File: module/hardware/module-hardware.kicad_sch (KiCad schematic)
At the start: 26 parts

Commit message: Add loopback routing mux; add digital signals to headers
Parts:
- added R?: 10k, symbol Device:R
- U6: renamed from U?; footprint (none) -> Package_SO:VSSOP-8_2.3x2mm_P0.5mm
- gave numbers to parts that had none: 25
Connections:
- net GNDD is gone; now on net GND: C1.2, C10.2, C2.2, C3.2, C4.2, C9.2, J1.5 (GND), J1.6 (Shield), J2.22 (Pin_22), J2.23 (Pin_23), J2.26 (Pin_26), J2.27 (Pin_27), J2.30 (Pin_30), J2.31 (Pin_31), J2.34 (Pin_34), J2.35 (Pin_35), J2.38 (Pin_38), J2.39 (Pin_39), SW1.1, U1.1 (GND), U4.10 (DGND)
- net VCC is gone; now on net +3V3: U6.8 (VCC)
- net +5VD: now also J2.32 (Pin_32), J4.24 (Pin_24), J4.25 (Pin_25)
- net GND: now also J4.22 (Pin_22), J4.23 (Pin_23), J4.26 (Pin_26), J4.27 (Pin_27), J4.30 (Pin_30), J4.31 (Pin_31), J4.34 (Pin_34), J4.35 (Pin_35), J4.38 (Pin_38), J4.39 (Pin_39), U6.2, R?.2
- net CBUS_SDRETOUT: now reaches U6.1
- net CBUS_SDRETOUT: now also J2.29 (Pin_29)
- net CBUS_NEXTPRSNT: now reaches U6.5
- net CBUS_NEXTPRSNT: now also J4.32 (Pin_32), R?.1
- net CBUS_SDRETIN: now reaches U6.6
- net CBUS_SDRETIN: now also J4.29 (Pin_29)
- net CBUS_SDOUT: now reaches U6.7
- net CBUS_SDOUT: now also J4.33 (Pin_33)
- net CBUS_SCK: now reaches J4.36 (Pin_36)
- net CBUS_SCK: now also J2.36 (Pin_36)
- net CBUS_DRDY: now reaches J4.37 (Pin_37)
- net CBUS_DRDY: now also J2.37 (Pin_37)
- net CBUS_EXTRA: now reaches J4.40 (Pin_40)
- net CBUS_EXTRA: now also J2.40 (Pin_40)
- net CBUS_SDIN: now reaches J2.33 (Pin_33)
- no-connect marks 1 -> 3
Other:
- sheet D.R.U.M. Module Digital ports: added GPIO16_EXTRA, GPIO17_DRDY, GPIO18_SCK, GPIO19_SDIN, GPIO20_SDOUT; removed none
- note added: "Data bus loopback routing mux"
- moved on the sheet: J4, U6A

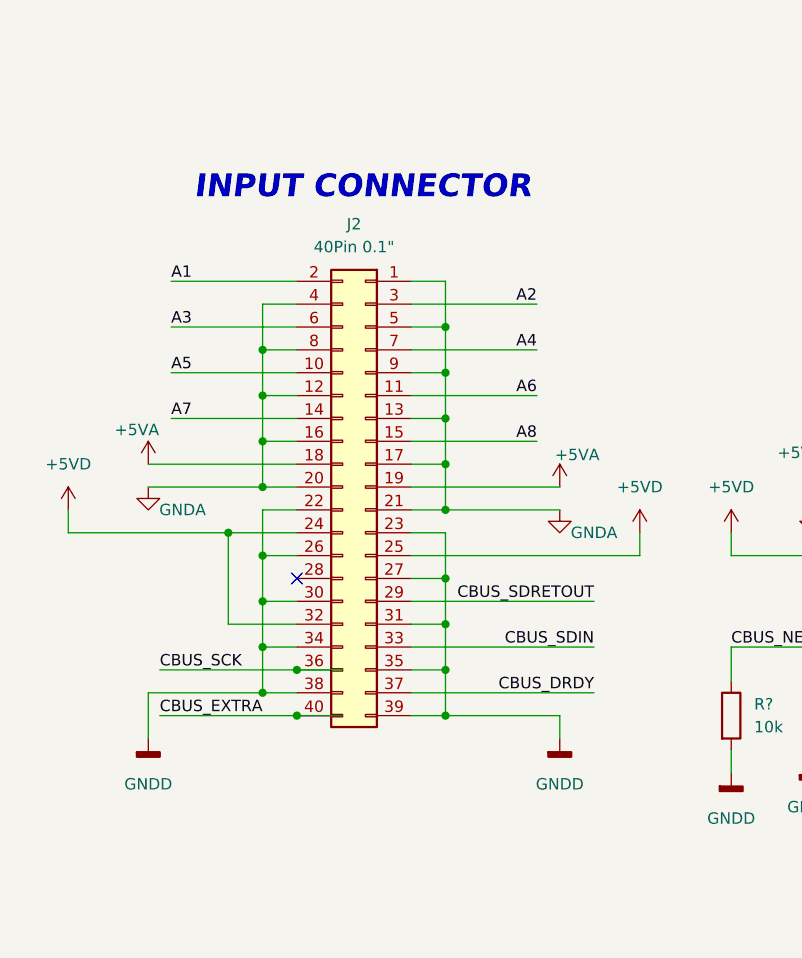
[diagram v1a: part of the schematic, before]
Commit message: Added pull-down resistors to analog passthroughs
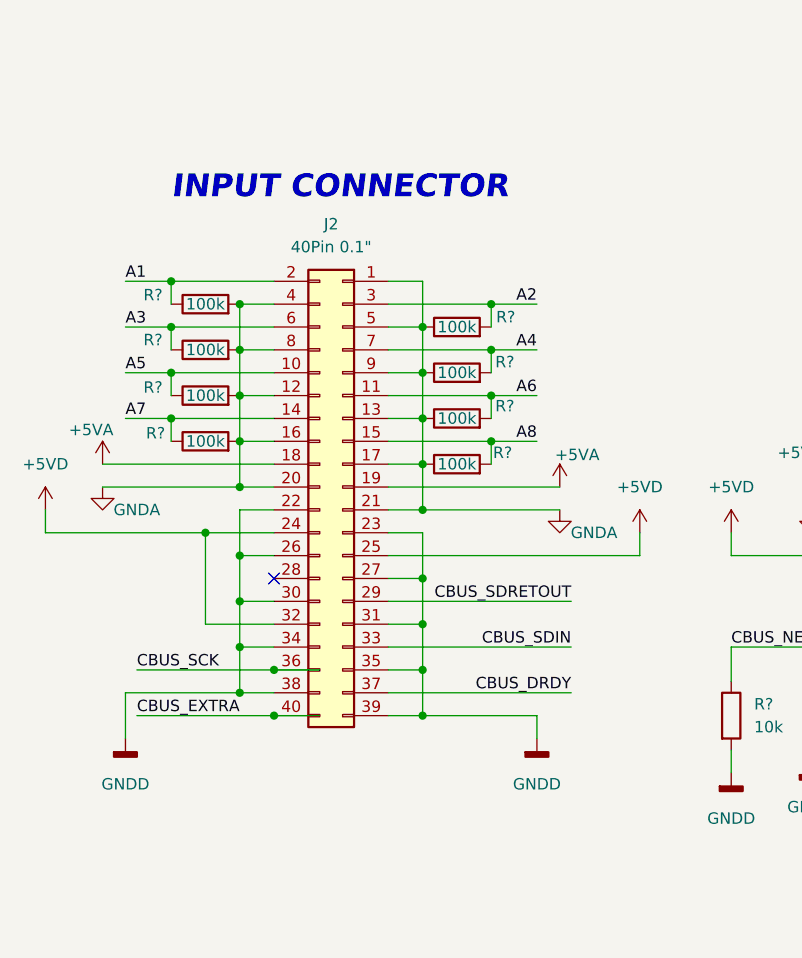
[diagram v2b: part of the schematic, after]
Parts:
- added R? (x8): 100k, symbol Device:R
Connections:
- net A1: now also R?.1
- net A2: now also R?.2
- net A3: now also R?.1
- net A4: now also R?.2
- net A5: now also R?.1
- net A6: now also R?.2
- net A7: now also R?.1
- net A8: now also R?.2
- net GNDA: now also R?.1, R?.1, R?.1, R?.1, R?.2, R?.2, R?.2, R?.2
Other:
- moved on the sheet: J2

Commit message: Add ADC vref, encoder & button headers
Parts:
- added C10, C13, C9: 0.1u, symbol Device:C
- added U5: MAX6070, symbol custom-lib:MAX6070
- gave numbers to parts that had none: 9
- renumbered C9 to C11, C10 to C12, R1 to R10, R2 to R11, R3 to R12, R4 to R13, U6 to U4, U4 to U6, U5 to U7
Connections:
- net +3.3VA: now also C9.1, U5.3 (EN), U5.4 (IN)
- net +3V3: no longer U6.2 (REF)
- net GND: no longer U6.10 (DGND)
- net GNDA: now also U6.10 (DGND), C10.2, C13.2, C9.2, U5.2 (GND)
- new net: C13.1, U5.5 (OUTS), U5.6 (OUTF), U6.2 (REF)
- new net: C10.1, U5.1 (FILTER)
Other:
- note removed: "NOTE: AGND and DGND must be tied together at this point"
- moved on the sheet: C11, C12, RV1, U4A, U6, U7

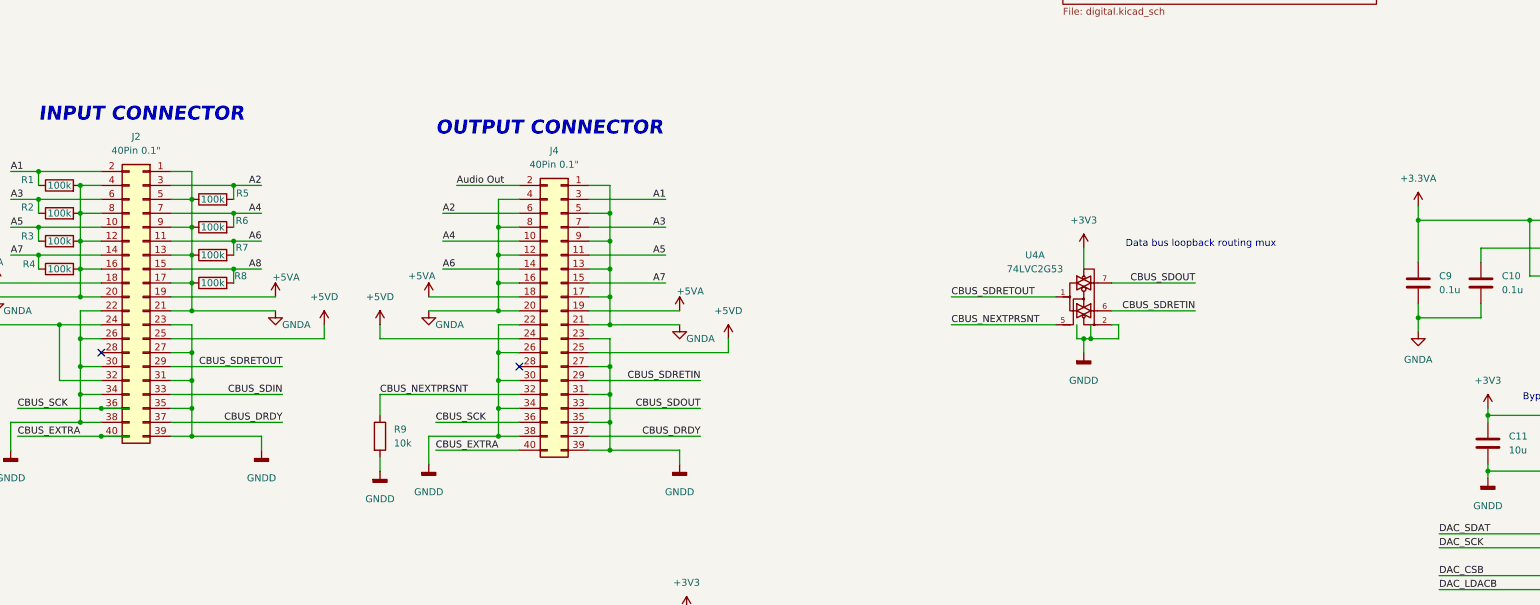
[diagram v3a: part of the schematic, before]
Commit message: Fix voltage rev supply (5V -> 3V3)
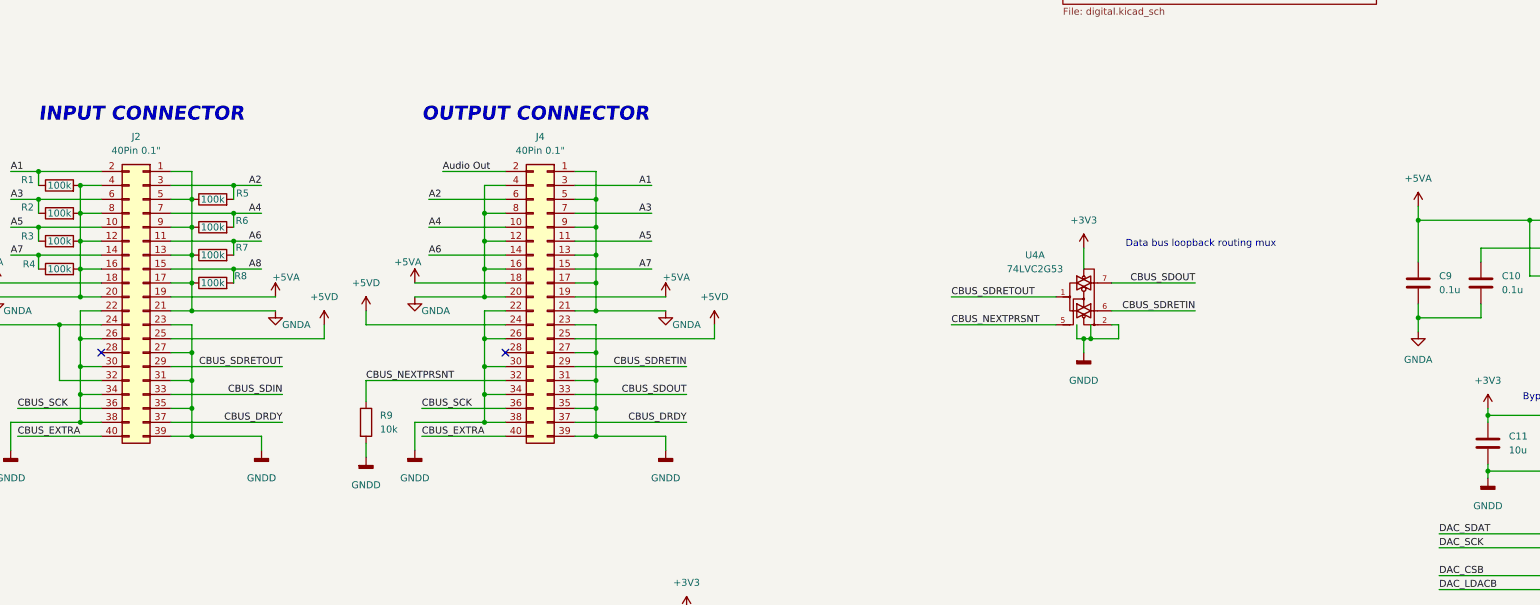
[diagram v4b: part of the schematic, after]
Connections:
- net +3.3VA: no longer C9.1, U5.3 (EN), U5.4 (IN)
- net +5VA: now also C9.1, U5.3 (EN), U5.4 (IN)
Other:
- moved on the sheet: J4, R9

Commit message: Add most footprints
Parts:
- C1, C11, C5: footprint (none) -> Capacitor_SMD:C_1206_3216Metric_Pad1.33x1.80mm_HandSolder
- C10, C12, C13, C2, C4, C6, C8, C9: footprint (none) -> Capacitor_SMD:C_0603_1608Metric_Pad1.08x0.95mm_HandSolder
- C3, C7: footprint (none) -> Capacitor_THT:CP_Radial_D8.0mm_P3.50mm
- J2: footprint (none) -> Connector_PinHeader_2.54mm:PinHeader_2x20_P2.54mm_Horizontal
- J3: footprint (none) -> Connector_PinHeader_2.54mm:PinHeader_1x02_P2.54mm_Horizontal
- J4: footprint (none) -> Connector_PinSocket_2.54mm:PinSocket_2x20_P2.54mm_Horizontal
- R1, R2, R3, R4, R5, R6, R7, R8: footprint (none) -> Resistor_SMD:R_1206_3216Metric_Pad1.30x1.75mm_HandSolder
- R10, R11, R13, R9: footprint (none) -> Resistor_SMD:R_0201_0603Metric_Pad0.64x0.40mm_HandSolder
- R12: footprint (none) -> Resistor_SMD:R_0603_1608Metric_Pad0.98x0.95mm_HandSolder
- U5: footprint (none) -> Package_TO_SOT_SMD:SOT-23-6_Handsoldering

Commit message: Finish footprint assignments; create cusom footprint lib
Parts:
- J1: footprint (none) -> Connector_USB:USB_Micro-B_Amphenol_10104110_Horizontal
- RV1: footprint (none) -> Potentiometer_THT:Potentiometer_Bourns_PTA6043_Single_Slide
- SW1: footprint (none) -> custom:TE_ConnMSLPT5252CG1
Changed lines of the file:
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@@
     (property "Reference" "SW1" (id 0) (at 139.7 199.39 0))
     (property "Value" "SW_Push" (id 1) (at 139.7 201.93 0))
-    (property "Footprint" "" (id 2) (at 139.7 201.93 0)
+    (property "Footprint" "custom:TE_ConnMSLPT5252CG1" (id 2) (at 139.7 201.93 0)
       (effects (font (size 1.27 1.27)) hide)
     )
@@
       (effects (font (size 1.27 1.27)) (justify right))
     )
-    (property "Footprint" "" (id 2) (at 360.68 171.45 0)
+    (property "Footprint" "Potentiometer_THT:Potentiometer_Bourns_PTA6043_Single_Slide" (id 2) (at 360.68 171.45 0)
       (effects (font (size 1.27 1.27)) hide)
     )
@@
     (property "Reference" "J1" (id 0) (at 31.75 190.5 0))
     (property "Value" "USB_B_Micro" (id 1) (at 31.75 193.04 0))
-    (property "Footprint" "" (id 2) (at 35.56 204.47 0)
+    (property "Footprint" "Connector_USB:USB_Micro-B_Amphenol_10104110_Horizontal" (id 2) (at 35.56 204.47 0)
       (effects (font (size 1.27 1.27)) hide)
     )
@@
     )
     (path "/c64d0991-6666-40ad-8f53-c4ec2d5065e9"
-      (reference "J1") (unit 1) (value "USB_B_Micro") (footprint "")
+      (reference "J1") (unit 1) (value "USB_B_Micro") (footprint "Connector_USB:USB_Micro-B_Amphenol_10104110_Horizontal")
     )
     (path "/d067ccfc-7346-4531-8a45-4ec88728c2e4"
@@
     )
     (path "/b169d545-bdb0-46f0-9e8e-232b739be3d3"
-      (reference "RV1") (unit 1) (value "10k Linear Pot") (footprint "")
+      (reference "RV1") (unit 1) (value "10k Linear Pot") (footprint "Potentiometer_THT:Potentiometer_Bourns_PTA6043_Single_Slide")
     )
     (path "/59c5fdd4-0275-4651-851a-34879fe6317f"
-      (reference "SW1") (unit 1) (value "SW_Push") (footprint "")
+      (reference "SW1") (unit 1) (value "SW_Push") (footprint "custom:TE_ConnMSLPT5252CG1")
     )
     (path "/8bf4dbf7-8f8f-435d-919b-c3a7dd1cb571/c3b0ca1c-76c1-4f22-a9a4-4f2d2d26349d"
-      (reference "SW2") (unit 1) (value "SW_Push") (footprint "")
+      (reference "SW2") (unit 1) (value "SW_Push") (footprint "custom:TE_ConnMSLPT5252CG1")
     )
     (path "/9c728db0-69af-414d-a337-b8d8f91d4481"

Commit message: Fix header footprints
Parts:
- J2: footprint Connector_PinHeader_2.54mm:PinHeader_2x20_P2.54mm_Horizontal -> Connector_PinSocket_2.54mm:PinSocket_2x20_P2.54mm_Horizontal
- J3: footprint Connector_PinHeader_2.54mm:PinHeader_1x02_P2.54mm_Horizontal -> Connector_PinHeader_2.54mm:PinHeader_1x02_P2.54mm_Vertical
- J4: footprint Connector_PinSocket_2.54mm:PinSocket_2x20_P2.54mm_Horizontal -> Connector_PinHeader_2.54mm:PinHeader_2x20_P2.54mm_Horizontal
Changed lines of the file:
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@@
     (property "Reference" "J4" (id 0) (at 123.19 88.9 0))
     (property "Value" "40Pin 0.1\"" (id 1) (at 123.19 91.44 0))
-    (property "Footprint" "Connector_PinSocket_2.54mm:PinSocket_2x20_P2.54mm_Horizontal" (id 2) (at 124.46 118.11 0)
+    (property "Footprint" "Connector_PinHeader_2.54mm:PinHeader_2x20_P2.54mm_Horizontal" (id 2) (at 124.46 118.11 0)
       (effects (font (size 1.27 1.27)) hide)
     )
@@
     (property "Reference" "J2" (id 0) (at 49.53 88.9 0))
     (property "Value" "40Pin 0.1\"" (id 1) (at 49.53 91.44 0))
-    (property "Footprint" "Connector_PinHeader_2.54mm:PinHeader_2x20_P2.54mm_Horizontal" (id 2) (at 50.8 118.11 0)
+    (property "Footprint" "Connector_PinSocket_2.54mm:PinSocket_2x20_P2.54mm_Horizontal" (id 2) (at 50.8 118.11 0)
       (effects (font (size 1.27 1.27)) hide)
     )
@@
       (effects (font (size 1.27 1.27)) (justify left))
     )
-    (property "Footprint" "Connector_PinHeader_2.54mm:PinHeader_1x02_P2.54mm_Horizontal" (id 2) (at 55.88 190.5 0)
+    (property "Footprint" "Connector_PinHeader_2.54mm:PinHeader_1x02_P2.54mm_Vertical" (id 2) (at 55.88 190.5 0)
       (effects (font (size 1.27 1.27)) hide)
     )
@@
     )
     (path "/d067ccfc-7346-4531-8a45-4ec88728c2e4"
-      (reference "J2") (unit 1) (value "40Pin 0.1\"") (footprint "Connector_PinHeader_2.54mm:PinHeader_2x20_P2.54mm_Horizontal")
+      (reference "J2") (unit 1) (value "40Pin 0.1\"") (footprint "Connector_PinSocket_2.54mm:PinSocket_2x20_P2.54mm_Horizontal")
     )
     (path "/f504757a-edf5-49c0-aaf8-9dd430fa0452"
-      (reference "J3") (unit 1) (value "Conn_01x02_Male") (footprint "Connector_PinHeader_2.54mm:PinHeader_1x02_P2.54mm_Horizontal")
+      (reference "J3") (unit 1) (value "Conn_01x02_Male") (footprint "Connector_PinHeader_2.54mm:PinHeader_1x02_P2.54mm_Vertical")
     )
     (path "/ccf0bcda-628a-4d14-84d6-36fa7b081e9b"
-      (reference "J4") (unit 1) (value "40Pin 0.1\"") (footprint "Connector_PinSocket_2.54mm:PinSocket_2x20_P2.54mm_Horizontal")
+      (reference "J4") (unit 1) (value "40Pin 0.1\"") (footprint "Connector_PinHeader_2.54mm:PinHeader_2x20_P2.54mm_Horizontal")
     )
     (path "/8bf4dbf7-8f8f-435d-919b-c3a7dd1cb571/051650c5-fe22-4d0f-87b8-0b3c8717c34d"
-      (reference "J5") (unit 1) (value "Conn_01x03_Male") (footprint "Connector_PinHeader_2.54mm:PinHeader_1x03_P2.54mm_Horizontal")
+      (reference "J5") (unit 1) (value "Conn_01x03_Male") (footprint "Connector_PinHeader_2.54mm:PinHeader_1x03_P2.54mm_Vertical")
     )
     (path "/8bf4dbf7-8f8f-435d-919b-c3a7dd1cb571/2fd0ee04-de1f-4e45-b88e-3fd404356e94"
-      (reference "J6") (unit 1) (value "Conn_01x03_Male") (footprint "Connector_PinHeader_2.54mm:PinHeader_1x03_P2.54mm_Horizontal")
+      (reference "J6") (unit 1) (value "Conn_01x03_Male") (footprint "Connector_PinHeader_2.54mm:PinHeader_1x03_P2.54mm_Vertical")
     )
     (path "/8bf4dbf7-8f8f-435d-919b-c3a7dd1cb571/02d63e74-12a7-47ea-8972-ec46cad19985"
-      (reference "J7") (unit 1) (value "Conn_01x03") (footprint "Connector_PinHeader_2.54mm:PinHeader_1x03_P2.54mm_Horizontal")
+      (reference "J7") (unit 1) (value "Conn_01x03") (footprint "Connector_PinHeader_2.54mm:PinHeader_1x03_P2.54mm_Vertical")
     )
     (path "/8bf4dbf7-8f8f-435d-919b-c3a7dd1cb571/650f2836-d59c-4d33-9218-d5e0bd831be2"
-      (reference "J8") (unit 1) (value "Conn_01x03") (footprint "Connector_PinHeader_2.54mm:PinHeader_1x03_P2.54mm_Horizontal")
+      (reference "J8") (unit 1) (value "Conn_01x03") (footprint "Connector_PinHeader_2.54mm:PinHeader_1x03_P2.54mm_Vertical")
     )
     (path "/8bf4dbf7-8f8f-435d-919b-c3a7dd1cb571/b3e5b5e6-c254-4fcf-9b58-13064dcb58be"
-      (reference "J9") (unit 1) (value "Conn_01x05_Male") (footprint "Connector_PinHeader_2.54mm:PinHeader_1x05_P2.54mm_Horizontal")
+      (reference "J9") (unit 1) (value "Conn_01x05_Male") (footprint "Connector_PinHeader_2.54mm:PinHeader_1x05_P2.54mm_Vertical")
     )
     (path "/8bf4dbf7-8f8f-435d-919b-c3a7dd1cb571/51e28174-fa87-4d2d-a642-5cb8c3b38549"
-      (reference "J10") (unit 1) (value "Conn_01x03") (footprint "Connector_PinHeader_2.54mm:PinHeader_1x03_P2.54mm_Horizontal")
+      (reference "J10") (unit 1) (value "Conn_01x03") (footprint "Connector_PinHeader_2.54mm:PinHeader_1x03_P2.54mm_Vertical")
     )
     (path "/8bf4dbf7-8f8f-435d-919b-c3a7dd1cb571/5e2ba949-280f-46dc-ae0f-3a65e906e7ac"
-      (reference "J11") (unit 1) (value "Conn_01x03") (footprint "Connector_PinHeader_2.54mm:PinHeader_1x03_P2.54mm_Horizontal")
+      (reference "J11") (unit 1) (value "Conn_01x03") (footprint "Connector_PinHeader_2.54mm:PinHeader_1x03_P2.54mm_Vertical")
     )
     (path "/8bf4dbf7-8f8f-435d-919b-c3a7dd1cb571/3bfb94ad-1214-4f13-b8ca-b203b4c98375"
-      (reference "J12") (unit 1) (value "Conn_01x03") (footprint "Connector_PinHeader_2.54mm:PinHeader_1x03_P2.54mm_Horizontal")
+      (reference "J12") (unit 1) (value "Conn_01x03") (footprint "Connector_PinHeader_2.54mm:PinHeader_1x03_P2.54mm_Vertical")
     )
     (path "/491c57aa-41d1-48a4-b426-df58ba28f05f"

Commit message: Begin layout process for module
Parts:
- R10, R11, R13, R9: footprint Resistor_SMD:R_0201_0603Metric_Pad0.64x0.40mm_HandSolder -> Resistor_SMD:R_0603_1608Metric_Pad0.98x0.95mm_HandSolder
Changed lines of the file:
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@@
       (effects (font (size 1.27 1.27)) (justify left))
     )
-    (property "Footprint" "Resistor_SMD:R_0201_0603Metric_Pad0.64x0.40mm_HandSolder" (id 2) (at 148.082 185.42 90)
+    (property "Footprint" "Resistor_SMD:R_0603_1608Metric_Pad0.98x0.95mm_HandSolder" (id 2) (at 148.082 185.42 90)
       (effects (font (size 1.27 1.27)) hide)
     )
@@
     (property "Reference" "R13" (id 0) (at 204.47 215.9 90))
     (property "Value" "10k" (id 1) (at 204.47 213.36 90))
-    (property "Footprint" "Resistor_SMD:R_0201_0603Metric_Pad0.64x0.40mm_HandSolder" (id 2) (at 204.47 211.582 90)
+    (property "Footprint" "Resistor_SMD:R_0603_1608Metric_Pad0.98x0.95mm_HandSolder" (id 2) (at 204.47 211.582 90)
       (effects (font (size 1.27 1.27)) hide)
     )
@@
       (effects (font (size 1.27 1.27)) (justify left))
     )
-    (property "Footprint" "Resistor_SMD:R_0201_0603Metric_Pad0.64x0.40mm_HandSolder" (id 2) (at 89.662 140.97 90)
+    (property "Footprint" "Resistor_SMD:R_0603_1608Metric_Pad0.98x0.95mm_HandSolder" (id 2) (at 89.662 140.97 90)
       (effects (font (size 1.27 1.27)) hide)
     )
@@
       (effects (font (size 1.27 1.27)) (justify left))
     )
-    (property "Footprint" "Resistor_SMD:R_0201_0603Metric_Pad0.64x0.40mm_HandSolder" (id 2) (at 193.802 185.42 90)
+    (property "Footprint" "Resistor_SMD:R_0603_1608Metric_Pad0.98x0.95mm_HandSolder" (id 2) (at 193.802 185.42 90)
       (effects (font (size 1.27 1.27)) hide)
     )
@@
     )
     (path "/dd6d8557-a6f2-47aa-9f09-b6b5a2e69b4f"
-      (reference "R9") (unit 1) (value "10k") (footprint "Resistor_SMD:R_0201_0603Metric_Pad0.64x0.40mm_HandSolder")
+      (reference "R9") (unit 1) (value "10k") (footprint "Resistor_SMD:R_0603_1608Metric_Pad0.98x0.95mm_HandSolder")
     )
     (path "/0b25ac29-e066-483d-ac3e-afa054824fd1"
-      (reference "R10") (unit 1) (value "10k") (footprint "Resistor_SMD:R_0201_0603Metric_Pad0.64x0.40mm_HandSolder")
+      (reference "R10") (unit 1) (value "10k") (footprint "Resistor_SMD:R_0603_1608Metric_Pad0.98x0.95mm_HandSolder")
     )
     (path "/f746e5c6-794b-4468-b212-0df7e89470c2"
-      (reference "R11") (unit 1) (value "10k") (footprint "Resistor_SMD:R_0201_0603Metric_Pad0.64x0.40mm_HandSolder")
+      (reference "R11") (unit 1) (value "10k") (footprint "Resistor_SMD:R_0603_1608Metric_Pad0.98x0.95mm_HandSolder")
     )
     (path "/d0a308a0-7a28-4730-859b-0a255eb0e81b"
@@
     )
     (path "/2af3ec11-05e7-41ef-8c7f-9ce653735e0c"
-      (reference "R13") (unit 1) (value "10k") (footprint "Resistor_SMD:R_0201_0603Metric_Pad0.64x0.40mm_HandSolder")
+      (reference "R13") (unit 1) (value "10k") (footprint "Resistor_SMD:R_0603_1608Metric_Pad0.98x0.95mm_HandSolder")
     )
     (path "/8bf4dbf7-8f8f-435d-919b-c3a7dd1cb571/7f93413a-b6ee-4a5f-90ed-213e55fb3d4a"
-      (reference "R14") (unit 1) (value "10k") (footprint "Resistor_SMD:R_0201_0603Metric_Pad0.64x0.40mm_HandSolder")
+      (reference "R14") (unit 1) (value "10k") (footprint "Resistor_SMD:R_0603_1608Metric_Pad0.98x0.95mm_HandSolder")
     )
     (path "/8bf4dbf7-8f8f-435d-919b-c3a7dd1cb571/d5d985db-9bef-4ec3-9d7a-f4359ac26581"
